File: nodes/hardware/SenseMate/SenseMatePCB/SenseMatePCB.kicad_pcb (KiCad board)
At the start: 2 copper layers, 1 part

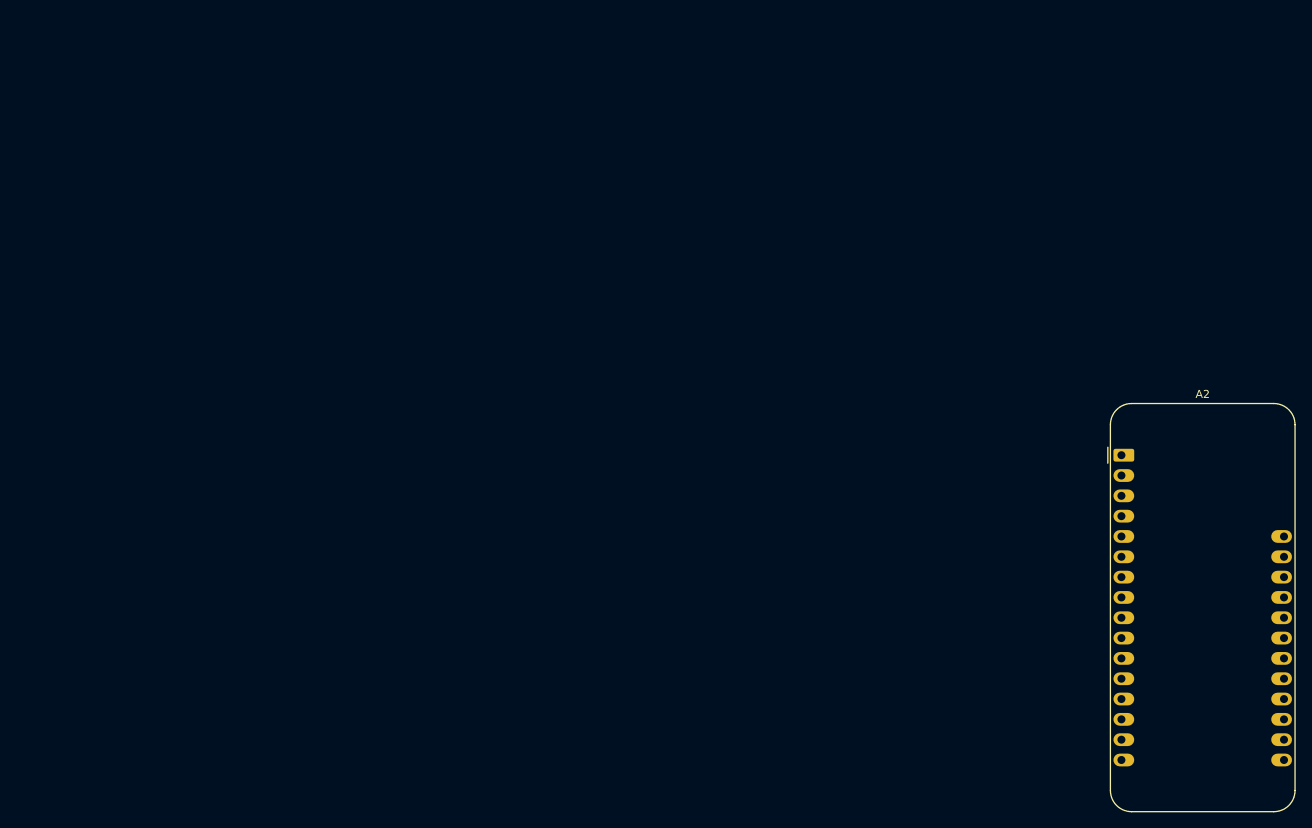
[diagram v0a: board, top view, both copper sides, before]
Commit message: revision of pcb and 3d design #27 #28
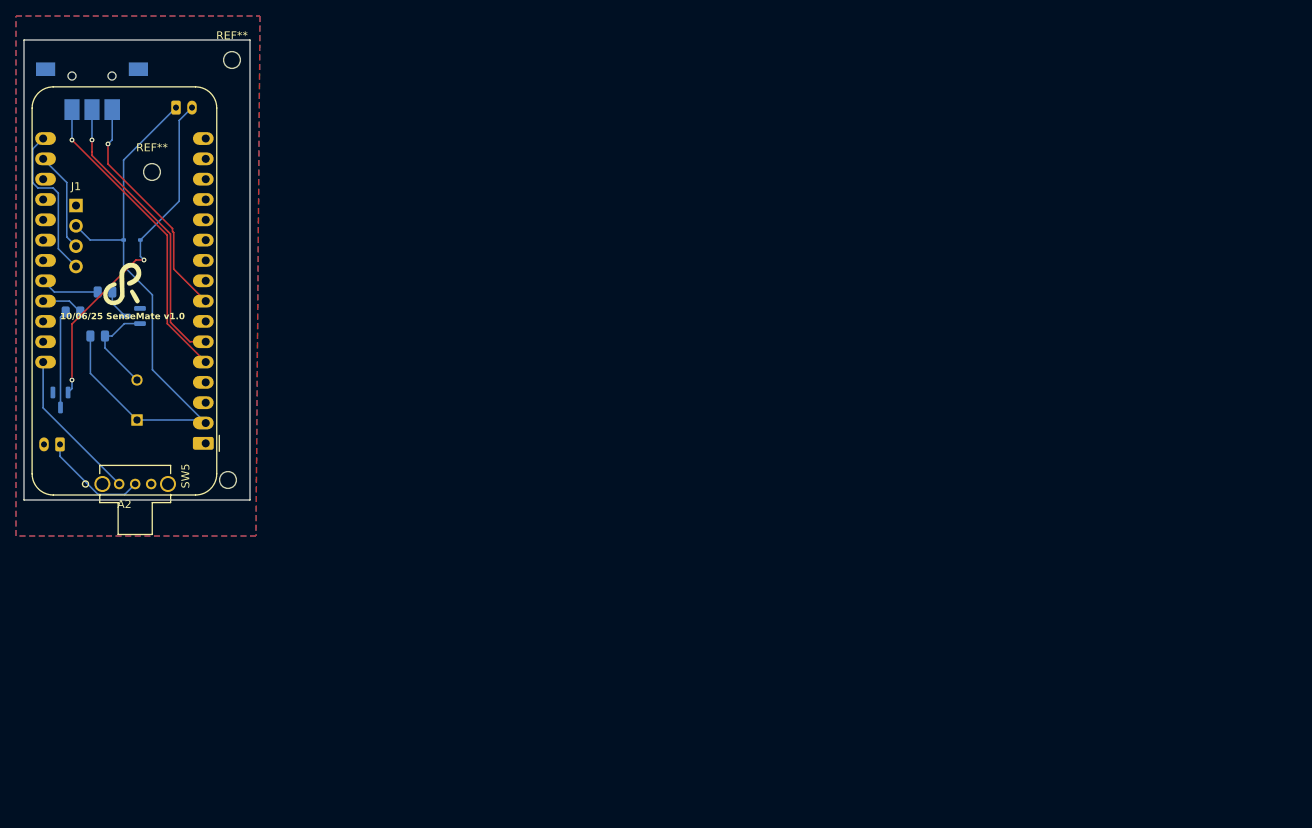
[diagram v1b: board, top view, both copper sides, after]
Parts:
- added BT1: Battery, Connector_JST:JST_PH_S2B-PH-K_1x02_P2.00mm_Horizontal, B.Cu at (97.5, 105.5)
- added D1: 1N4148, Diode_SMD:D_SOD-323, B.Cu at (106.5, 80.0)
- added G***: LOGO, LOGO, F.Cu at (107.8, 85.5)
- added J1: Conn_01x04, Connector_PinHeader_2.54mm:PinHeader_1x04_P2.54mm_Vertical, B.Cu at (99.5, 75.7)
- added M1: Motor_DC, Connector_JST:JST_PH_S2B-PH-K_1x02_P2.00mm_Horizontal, B.Cu at (112.0, 63.5)
- added Q1: 2SC1815, Package_TO_SOT_SMD:SOT-23, B.Cu at (106.6, 89.5)
- added Q2: 2SC1815, Package_TO_SOT_SMD:SOT-23, B.Cu at (97.6, 100.0)
- added R1: R, Resistor_SMD:R_0805_2012Metric, B.Cu at (102.2, 92.0)
- added R2: R, Resistor_SMD:R_0805_2012Metric, B.Cu at (103.1, 86.5)
- added R3: R, Resistor_SMD:R_0805_2012Metric, B.Cu at (99.1, 89.0)
- added REF**: MountingHole_2.1mm, MountingHole:MountingHole_2.1mm, F.Cu at (109.0, 71.5)
- added REF**: MountingHole_2.1mm, MountingHole:MountingHole_2.1mm, F.Cu at (119.0, 57.5)
- added REF**: MountingHole_2.1mm, MountingHole:MountingHole_2.1mm, F.Cu at (118.5, 110.0)
- added S1: COM-08184, SenseMate_sw_fp:COM08184, B.Cu at (101.5, 59.5)
- added SW5: SW_DPDT_x2, SenseMate_Pwr_Button_:OS102011MA1QN1, F.Cu at (104.9, 110.5)
- added XTAL1: CRYSTALH, SenseMate_sound:PS1240P02BT, B.Cu at (107.1, 102.5)
- moved A2 114.5 mm to (115.7, 105.4), turned to 180 degrees
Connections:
- A2 pad 17: unconnected-(A2-SDA-Pad17) -> Net-(A2-SDA)
- A2 pad 18: unconnected-(A2-SCL-Pad18) -> Net-(A2-SCL)
- A2 pad 19: unconnected-(A2-5-Pad19) -> LoRa_DIO1
- A2 pad 2: unconnected-(A2-3V3-Pad2) -> +3V3
- A2 pad 20: unconnected-(A2-6-Pad20) -> LoRa_DIO2
- A2 pad 21: unconnected-(A2-9-Pad21) -> LoRa_RST
- A2 pad 22: unconnected-(A2-10-Pad22) -> LoRa_CS
- A2 pad 23: unconnected-(A2-11-Pad23) -> LoRa_IRQ
- A2 pad 24: unconnected-(A2-12-Pad24) -> Net-(A2-12)
- A2 pad 25: unconnected-(A2-13-Pad25) -> Net-(A2-13)
- A2 pad 28: unconnected-(A2-VBAT-Pad28) -> Net-(A2-VBAT)
- A2 pad 4: unconnected-(A2-GND-Pad4) -> GND
- A2 pad 5: unconnected-(A2-A0-Pad5) -> Net-(A2-A0)
- A2 pad 6: unconnected-(A2-A1-Pad6) -> Net-(A2-A1)
- A2 pad 8: unconnected-(A2-A3-Pad8) -> Net-(A2-A3)
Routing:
- net +3V3: track 0.00 -> 74.7 mm
- net Net-(D1-A): track 0.00 -> 43.0 mm, vias 0 -> 2
- net Net-(A2-A0): track 0.00 -> 38.5 mm, vias 0 -> 1
- net Net-(A2-A1): track 0.00 -> 36.1 mm, vias 0 -> 1
- net Net-(A2-A3): track 0.00 -> 29.2 mm, vias 0 -> 1
- net Net-(A2-SDA): track 0.00 -> 19.9 mm
- net Net-(A2-VBAT): track 0.00 -> 19.2 mm
- net Net-(BT1-+): track 0.00 -> 13.4 mm
- net Net-(A2-SCL): track 0.00 -> 12.6 mm
- net Net-(Q2-B): track 0.00 -> 12.2 mm
- net Net-(Q1-C): track 0.00 -> 12.2 mm
- net Net-(A2-12): track 0.00 -> 7.40 mm
- net Net-(A2-13): track 0.00 -> 5.21 mm
- net Net-(Q1-B): track 0.00 -> 3.66 mm
- added copper zone on B.Cu, net GND
- added copper zone on F.Cu, net GND
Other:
- board outline added: 28.2 x 57.5 mm
- board text added: "10/06/25 SenseMate v1.0"

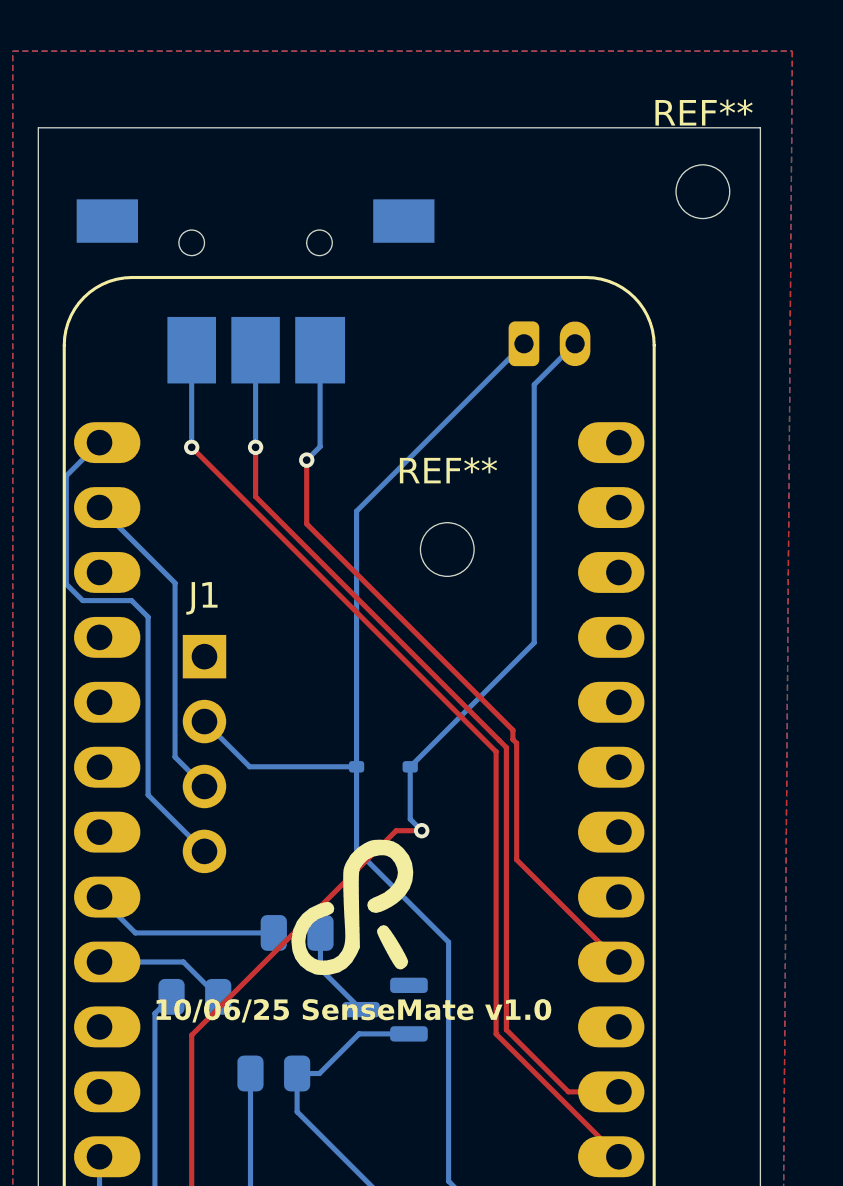
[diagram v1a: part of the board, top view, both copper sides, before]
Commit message: changed motor connector to 2-pin-header
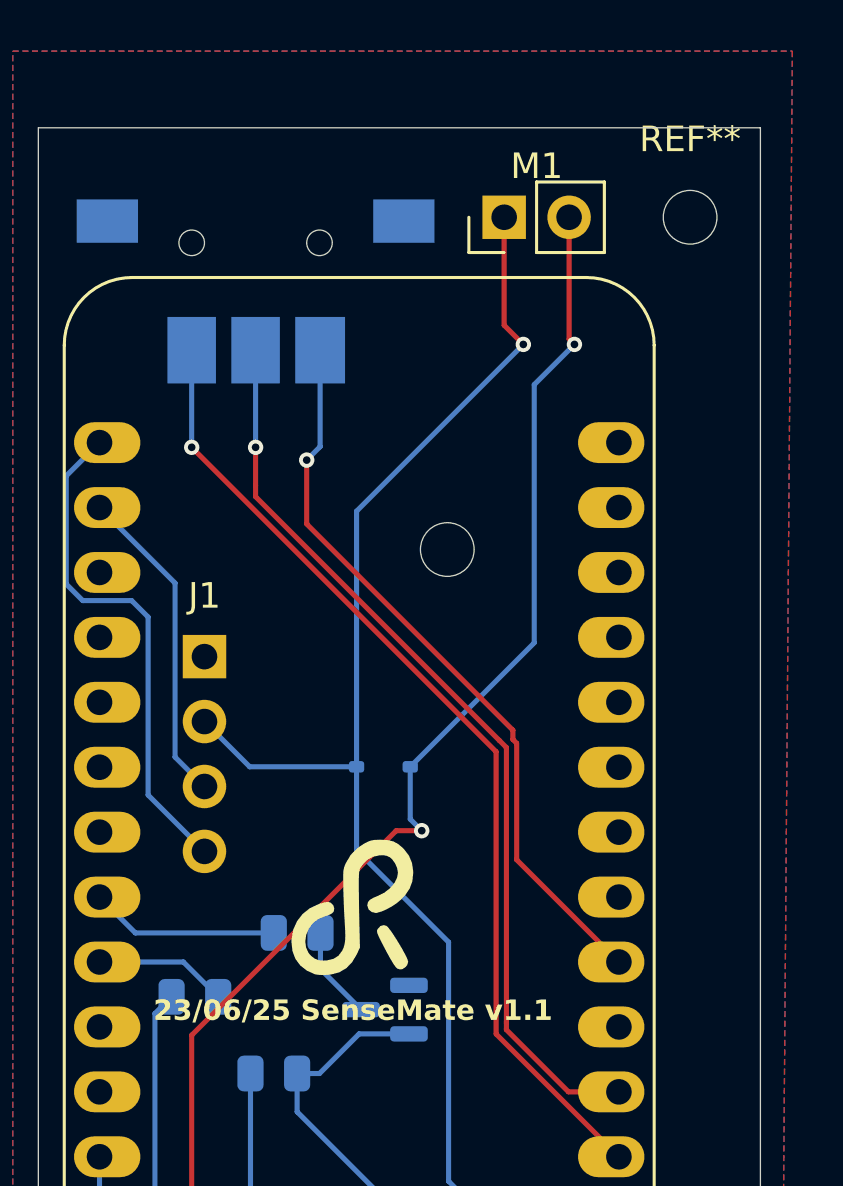
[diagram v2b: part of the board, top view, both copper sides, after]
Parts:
- M1: footprint Connector_JST:JST_PH_S2B-PH-K_1x02_P2.00mm_Horizontal -> Connector_PinHeader_2.54mm:PinHeader_1x02_P2.54mm_Vertical; moved to F.Cu
- moved M1 5.01 mm to (111.2, 58.5), turned to 90 degrees
- moved REF** 1.12 mm to (118.5, 58.5)
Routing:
- net +3V3: track 74.7 -> 80.0 mm, vias 0 -> 1
- net Net-(D1-A): track 43.0 -> 48.0 mm, vias 2 -> 3
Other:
- board text added: "23/06/25 SenseMate v1.1"
- board text removed: "10/06/25 SenseMate v1.0"
